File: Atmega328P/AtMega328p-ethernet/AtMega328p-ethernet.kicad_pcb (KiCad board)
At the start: 4 copper layers, 72.5 x 55 mm, 90 parts, among them J10 Conn_02x03_Counter_Clockwise, J2 USB_C_Receptacle_USB2.0_12P, J3 Conn_02x05_Odd_Even, J4 Conn_01x06_Socket, J5 Conn_01x06_Socket, J6 Conn_01x06_Socket, J7 Conn_01x06_Socket, J8 Conn_02x03_Counter_Clockwise, J9 RJ45_Hanrun_HR911105A_Horizon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, SW1 SW_Push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

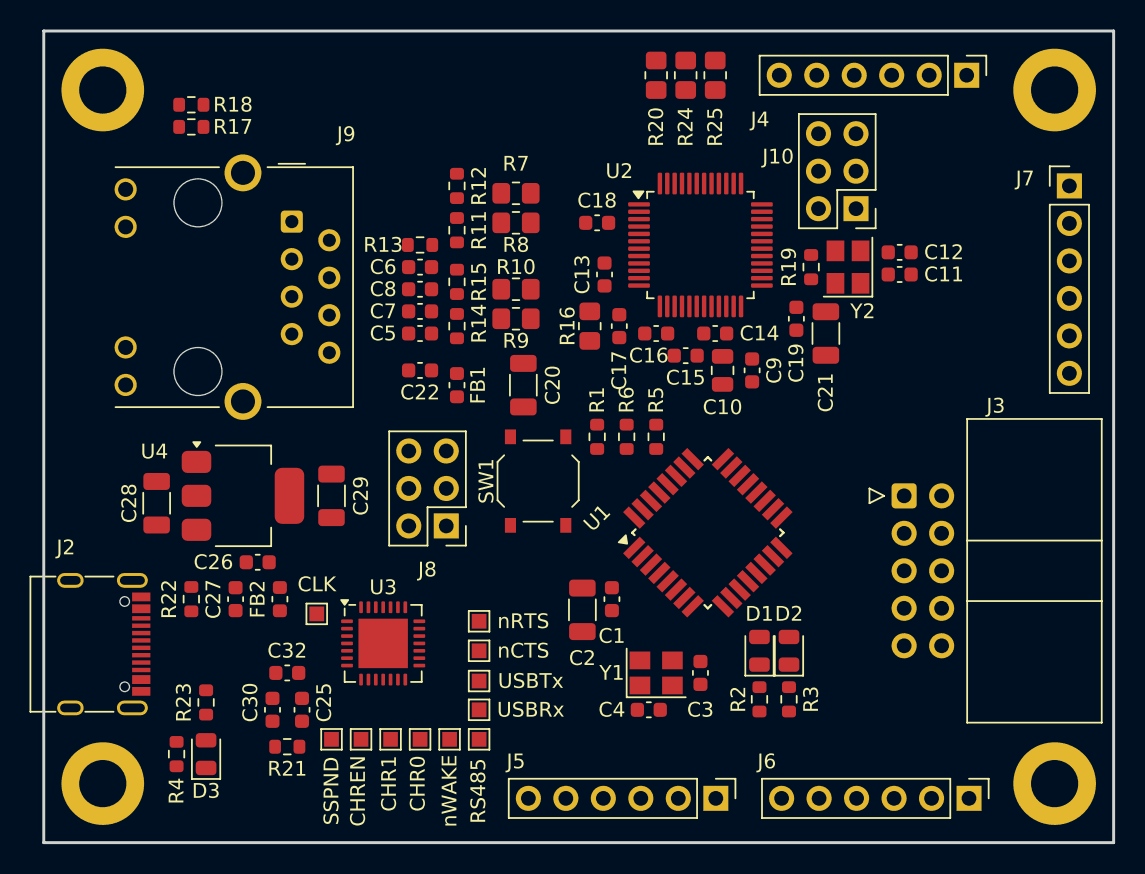
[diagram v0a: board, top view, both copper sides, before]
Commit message: Most traces complete just GPIO left
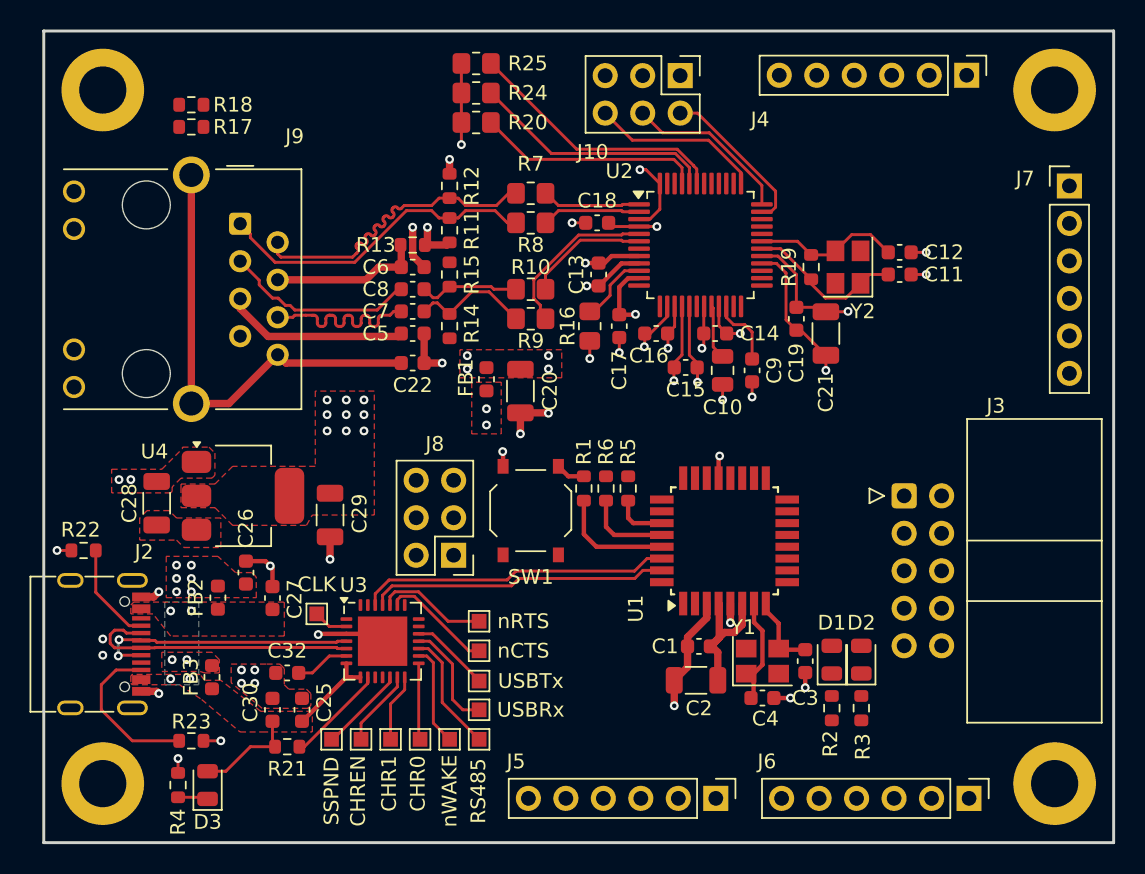
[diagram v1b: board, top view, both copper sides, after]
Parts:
- added FB3: 100R@100MHz, Inductor_SMD:L_0603_1608Metric, F.Cu at (111.4, 141.3)
- moved R25 16.2 mm to (129.3, 99.7), turned to 0 degrees
- moved J10 14.9 mm to (143.1, 100.5), turned to -90 degrees
- moved R24 14.3 mm to (129.3, 101.7), turned to 0 degrees
- moved R20 12.6 mm to (129.3, 103.7), turned to 0 degrees
- moved C2 9.06 mm to (144.2, 141.5), turned to 180 degrees
- moved R22 8.01 mm to (102.7, 132.7), turned to 0 degrees
- moved C4 7.74 mm to (148.7, 142.7)
- moved Y1 7.24 mm to (148.7, 140.2)
- moved C3 7.14 mm to (151.6, 140.2)
- moved C1 6.71 mm to (144.4, 139.2), turned to 180 degrees
- moved D1 4.94 mm to (153.4, 140.1)
- moved D2 4.94 mm to (155.4, 140.1)
- moved R2 4.94 mm to (153.4, 143.4)
- moved R3 4.94 mm to (155.4, 143.4)
- moved FB2 4.20 mm to (111.8, 135.9)
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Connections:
- net Net-(C7-Pad1) renamed /ETHERNET_MODULE/ETH_RX_I_N
- net Net-(C8-Pad1) renamed /ETHERNET_MODULE/ETH_RX_I_P
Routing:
- net GND: track 0.00 -> 81.2 mm, vias 0 -> 40
- net Net-(C22-Pad1): track 0.00 -> 31.3 mm
- net /ETHERNET_MODULE/+3.3VA_IN: track 0.00 -> 27.2 mm, vias 0 -> 12
- net /ETHERNET_MODULE/ETH_C_TX_P: track 0.00 -> 22.1 mm
- net /ETHERNET_MODULE/ETH_C_TX_N: track 0.00 -> 21.4 mm
- net /MCU_RXD: track 0.00 -> 21.2 mm
- net /MCU_TXD: track 0.00 -> 20.3 mm
- net /USB_INTERFACE/USB_N: track 0.00 -> 19.1 mm
- net /USB_INTERFACE/USB_P: track 0.00 -> 18.2 mm, vias 0 -> 2
- net Net-(U2-PMODE2): track 0.00 -> 17.9 mm
- net Net-(U2-PMODE1): track 0.00 -> 17.0 mm
- net Net-(U2-PMODE0): track 0.00 -> 15.3 mm
- net VBUS: track 0.00 -> 13.2 mm, vias 0 -> 4
- net /ETHERNET_MODULE/ETH_C_RX_P: track 0.00 -> 13.1 mm
- net /ETHERNET_MODULE/ETH_C_RX_N: track 0.00 -> 12.9 mm
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- added copper zone on F.Cu, net +3.3V
- added copper zone on F.Cu, net +5V
- added copper zone on F.Cu, net /ETHERNET_MODULE/+3.3VA_IN
- added copper zone on F.Cu, net GND
- added copper zone on B.Cu, net VBUS
- added copper zone on F.Cu, net VBUS

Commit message: Tracing complete ready for final check and silk screen.
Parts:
- added C23: 100nF, Capacitor_SMD:C_0603_1608Metric, F.Cu at (147.3, 125.3)
- moved D2 10.4 mm to (146.9, 146.1), turned to 0 degrees
- moved R3 8.75 mm to (146.7, 144.3), turned to 180 degrees
- moved D1 6.02 mm to (152.2, 146.0), turned to 180 degrees
- moved R18 1.73 mm to (109.7, 104.2)
- moved R17 1.33 mm to (109.7, 102.7)
- moved R2 1.29 mm to (152.4, 144.2), turned to 0 degrees
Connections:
- D1 pad 2: /PD6/LED1 -> /PD7/LED2
- D2 pad 2: /PD7/LED2 -> /PD6/LED1
- J3 pad 3: /SPI_MOSI -> /SPI_SCK
- J3 pad 4: /SDA -> /I2C_SDA
- J3 pad 6: /SCL -> /I2C_SCL
- J3 pad 7: /SPI_CLK -> /SPI_MOSI
- J5 pad 3: /PD2 -> /PD5
- J5 pad 4: /PD3 -> /PD4
- J5 pad 5: /PD4 -> /PD3
- J5 pad 6: /PD5 -> /PD2
- J6 pad 3: /PB0 -> /PB1
- J6 pad 4: /PB1 -> /PB0
- J6 pad 5: /PD6/LED1 -> /PD7/LED2
- J6 pad 6: /PD7/LED2 -> /PD6/LED1
- R5 pad 2: +5V -> +3.3V
- R6 pad 2: +5V -> +3.3V
- U1 pad 20: unconnected-(U1-AREF-Pad20) -> Net-(U1-AREF)
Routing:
- net /SPI_MOSI: track 0.00 -> 95.1 mm
- net /PC0: track 0.00 -> 89.5 mm, vias 0 -> 2
- net /SPI_MISO: track 0.00 -> 81.0 mm
- net /SPI_SCK: track 0.00 -> 79.9 mm
- net /PD5: track 0.00 -> 78.4 mm, vias 0 -> 2
- net /PB2: track 0.00 -> 50.8 mm, vias 0 -> 1
- net /PC3: track 0.00 -> 50.4 mm, vias 0 -> 1
- net /PC2: track 0.00 -> 48.4 mm, vias 0 -> 1
- net /ETHERNET_MODULE/ACTLED: track 0.00 -> 48.1 mm, vias 0 -> 2
- net /PC1: track 0.00 -> 46.4 mm, vias 0 -> 1
- net /ETHERNET_MODULE/LINKLED: track 0.00 -> 45.1 mm, vias 0 -> 2
- net /I2C_SCL: track 5.78 -> 47.0 mm, vias 0 -> 1
- net /I2C_SDA: track 3.60 -> 43.0 mm, vias 0 -> 1
- net /MCU_RXD: track 21.2 -> 57.1 mm, vias 0 -> 1
- net /MCU_TXD: track 20.3 -> 55.5 mm, vias 0 -> 1
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
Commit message: Ethernet atmega328p reviewed
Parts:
- moved C15 0.30 mm to (143.5, 120.0)
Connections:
- U2 pad 32: /SPI_SCK -> /ETH_SPI_SS
- U2 pad 33: /SPI_MISO -> /SPI_SCK
- U2 pad 34: /SPI_MOSI -> /SPI_MISO
- U2 pad 35: /ETH_SPI_SS -> /SPI_MOSI
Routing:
- net Net-(J9-RCT): track 12.6 -> 37.3 mm, vias 0 -> 2
- net GND: track 84.9 -> 93.9 mm
- net /ETH_SPI_SS: track 11.0 -> 17.4 mm, vias 0 -> 1
- net /PB2: track 50.8 -> 52.9 mm
- net /SPI_MISO: track 81.0 -> 80.4 mm
- net /SPI_SCK: track 79.9 -> 79.4 mm

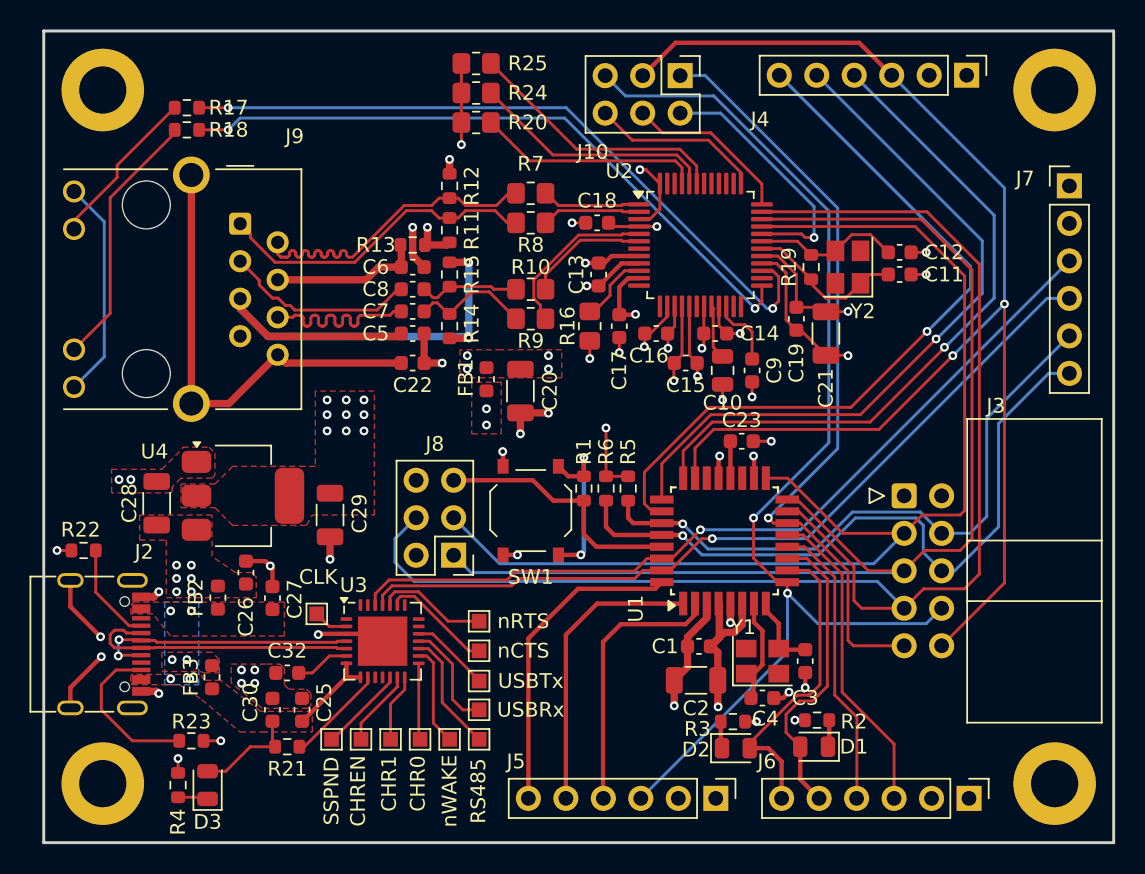
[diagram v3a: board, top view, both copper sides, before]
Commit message: Added pin descriptions
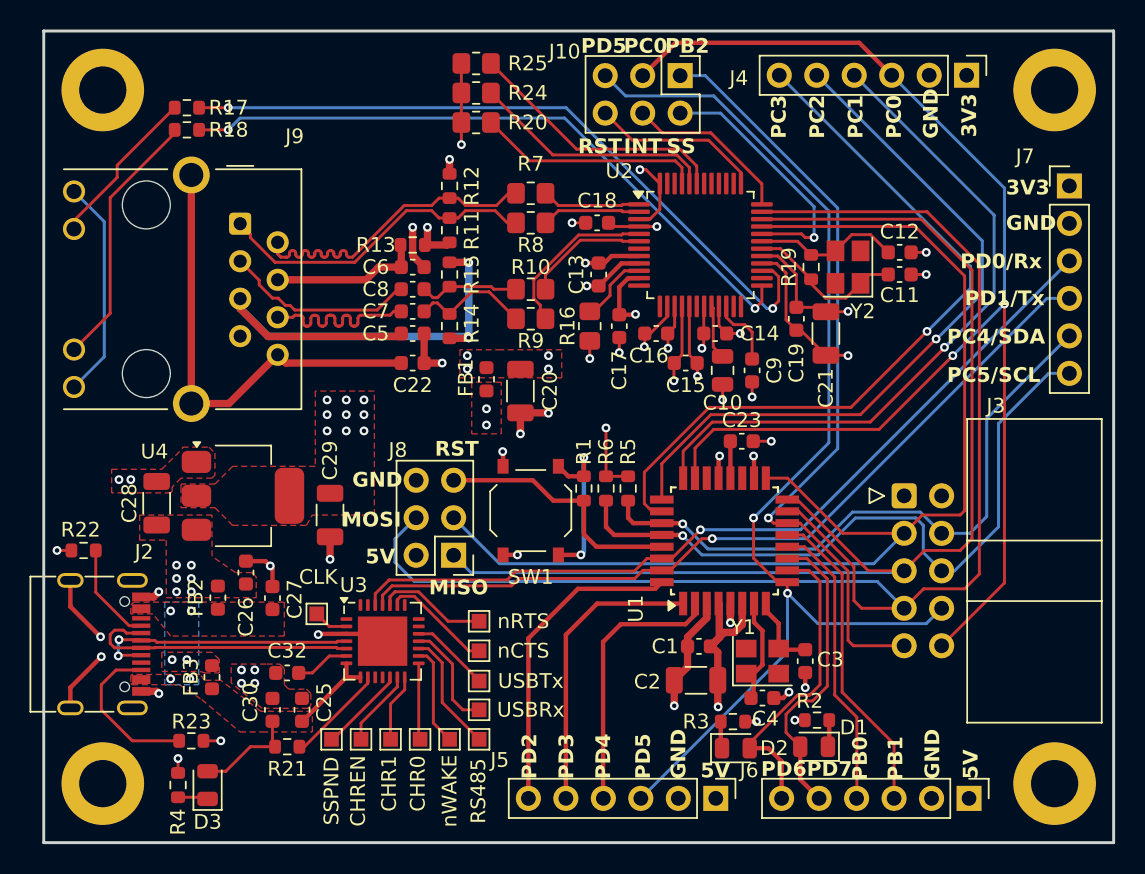
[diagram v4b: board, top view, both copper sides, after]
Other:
- board text added: "3V3"
- board text added: "5V"
- board text added: "GND"
- board text added: "INT"
- board text added: "MISO"
- board text added: "MOSI"
- board text added: "PB0"
- board text added: "PB1"
- board text added: "PB2"
- board text added: "PC0"
- board text added: "PC1"
- board text added: "PC2"
- board text added: "PC3"
- board text added: "PC4/SDA"
- board text added: "PC5/SCL"
- board text added: "PD0/Rx"
- board text added: "PD1/Tx"
- board text added: "PD2"
- board text added: "PD3"
- board text added: "PD4"
- board text added: "PD5"
- board text added: "PD6"
- board text added: "PD7"
- board text added: "RST"
- board text added: "SCK"
- board text added: "SCL"
- board text added: "SDA"
- board text added: "SS"
